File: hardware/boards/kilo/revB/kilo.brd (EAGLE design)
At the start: 100.3 x 100 mm, 35 parts, among them X1 STEREOJACK

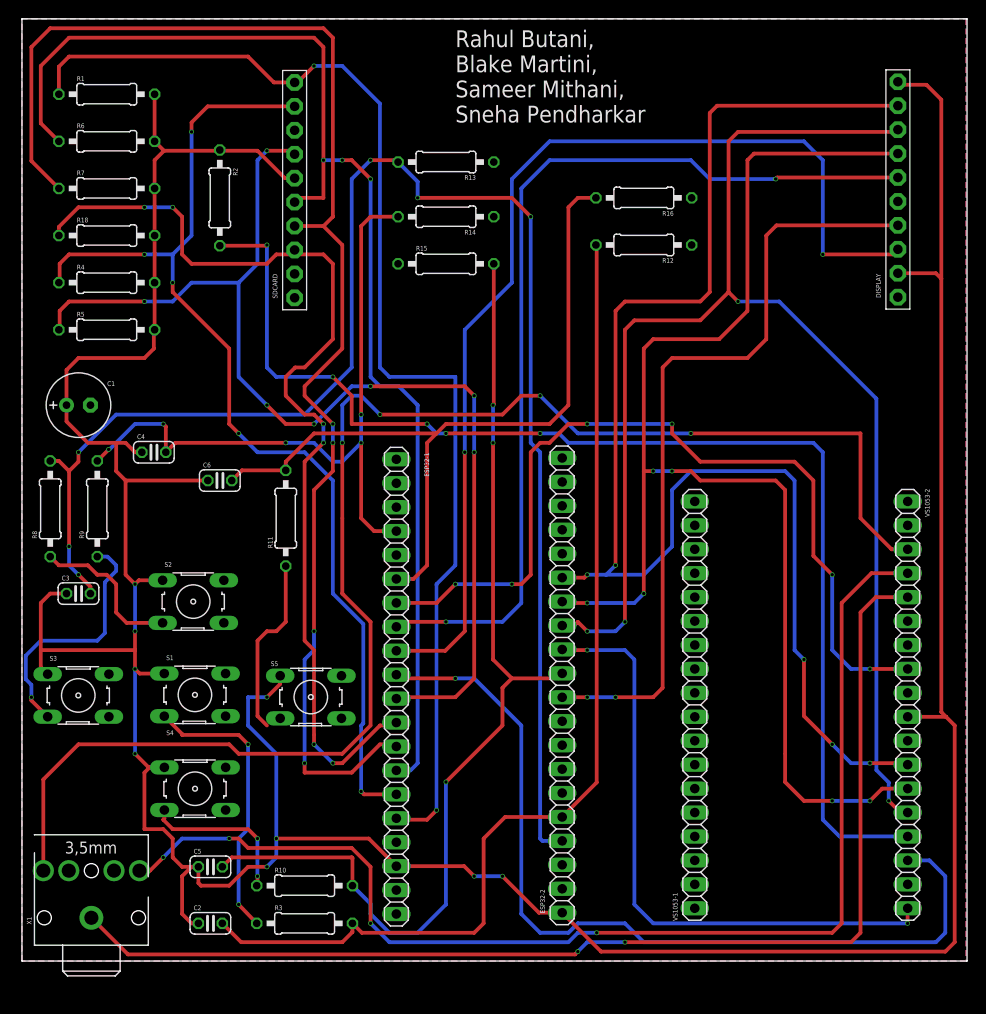
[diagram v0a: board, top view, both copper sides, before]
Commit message: Redo the board for kilo, revision B (aka the backup board)
Closes #17.
Closes #18.
Closes #19.
Closes #20.
Closes #21.
Closes #22.
Closes #23.
Closes #24.
Closes #25.
Closes #27.
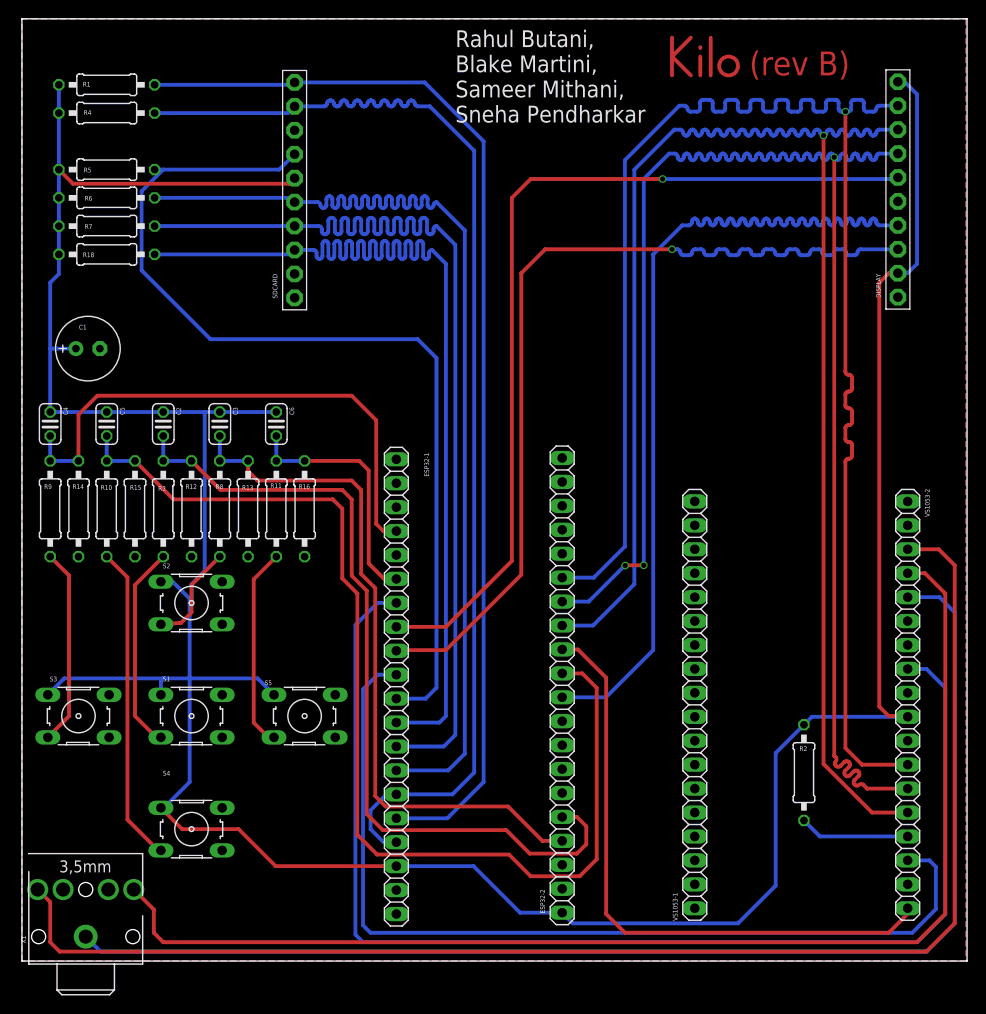
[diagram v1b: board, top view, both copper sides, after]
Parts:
- moved R2 87.0 mm to (83.0, 20.0)
- moved R12 55.6 mm to (18.0, 48.0), turned to 90 degrees
- moved C2 53.2 mm to (15.0, 57.0), turned to 270 degrees
- moved R14 49.8 mm to (6.00, 48.0), turned to 90 degrees
- moved R16 48.8 mm to (30.0, 48.0), turned to 90 degrees
- moved C5 48.3 mm to (9.00, 57.0), turned to 270 degrees
- moved R3 46.5 mm to (15.0, 48.0), turned to 90 degrees
- moved R10 45.2 mm to (9.00, 48.0), turned to 90 degrees
- moved R13 42.4 mm to (24.0, 48.0), turned to 90 degrees
- moved R15 42.0 mm to (12.0, 48.0), turned to 90 degrees
- moved C3 23.4 mm to (21.0, 57.0), turned to 270 degrees
- moved R4 18.0 mm to (9.00, 90.0), turned to 180 degrees
- moved R8 18.0 mm to (21.0, 48.0)
- moved R5 17.0 mm to (9.00, 84.0), turned to 180 degrees
- moved C4 11.4 mm to (3.00, 57.0), turned to 270 degrees
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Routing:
- net N$20: track 131.3 -> 11.7 mm, vias 5 -> 0
- net IO37: track 163.7 -> 74.5 mm, vias 6 -> 0
- net IO25: track 82.2 -> 26.4 mm
- net V3P3: track 382.4 -> 338.9 mm, vias 9 -> 0
- net DREQ: track 90.5 -> 131.2 mm, vias 6 -> 0
- net IO13: track 147.0 -> 114.6 mm, vias 4 -> 0
- net SPI_MOSI: track 141.3 -> 167.5 mm, vias 6 -> 3
- net IO38: track 111.3 -> 88.7 mm
- net SPI_MISO: track 150.4 -> 170.3 mm, vias 5 -> 1
- net IO15: track 133.3 -> 114.4 mm, vias 3 -> 0
- net DISPLAY_RST: track 111.9 -> 93.8 mm, vias 2 -> 1
- net SPI_CLK: track 151.9 -> 169.3 mm, vias 4 -> 1
- net IO14: track 118.9 -> 102.1 mm, vias 7 -> 0
- net N$24: track 16.9 -> 33.7 mm, vias 2 -> 0
- net SVP: track 74.2 -> 57.5 mm, vias 5 -> 0
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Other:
- board text added: "(rev B)"
